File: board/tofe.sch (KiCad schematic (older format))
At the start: 14 parts

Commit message: Moving I2C enable pins to make IO1 a NC.
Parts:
- removed PDG0: DEBUG, CON-SMD-2.54:TE-AMPMODU-MOD-II-4X2, symbol CONN_02X04
- added DDG3: LED, LEDs:LED_0805, symbol LED
- added PDG0: DEBUG, symbol CONN_02X05
- added RDG3: 68R, Resistors_SMD:R_0805_HandSoldering, symbol R
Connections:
- wire segments 136 -> 146
- no-connect marks 4 -> 5

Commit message: Updating PCB.
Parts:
- PDG0: footprint (none) -> Pin_Headers:Pin_Header_Straight_2x05
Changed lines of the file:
@@
 F 0 "PDG0" H 7050 3450 50  0000 C CNN
 F 1 "DEBUG" H 7050 2850 50  0000 C CNN
-F 2 "" H 7050 1950 50  0000 C CNN
+F 2 "Pin_Headers:Pin_Header_Straight_2x05" H 7050 1950 50  0001 C CNN
 F 3 "" H 7050 1950 50  0000 C CNN
 	1    7050 3150

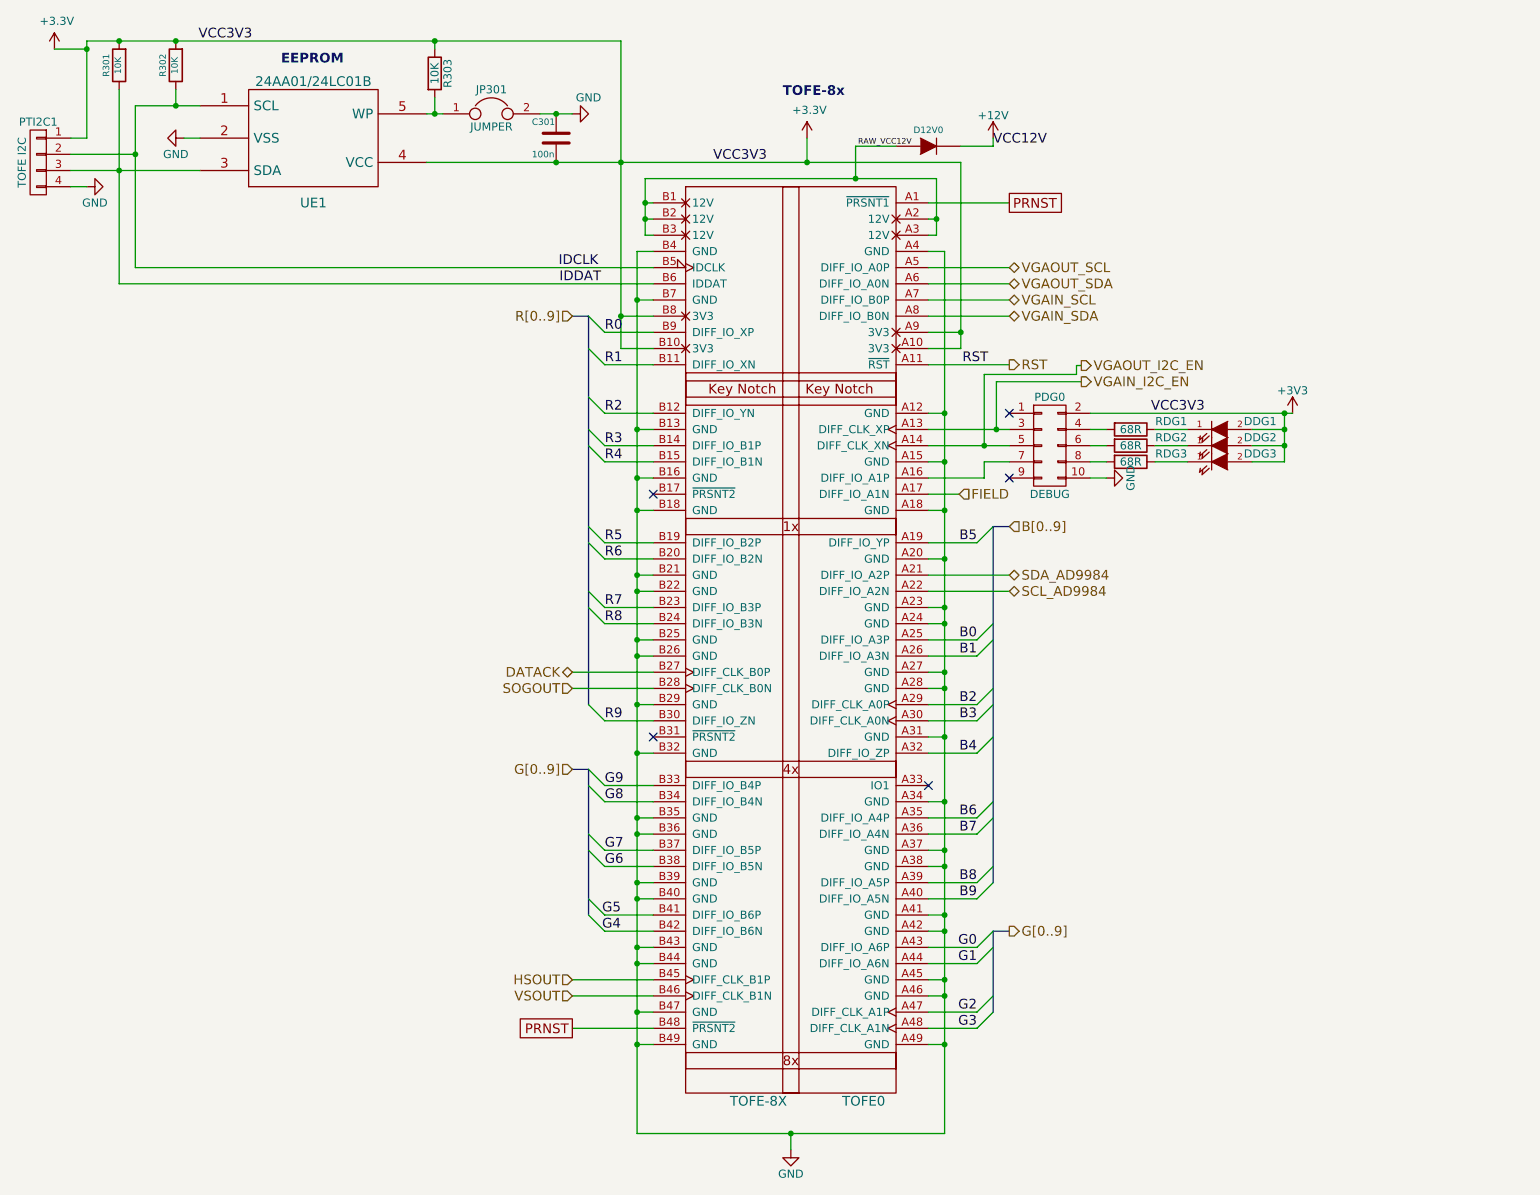
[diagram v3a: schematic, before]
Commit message: Change TOFE connections as per changes requested for PCB design
Note: `DATACK` & `SOGOUT` have been swapped from the original request
      keeping in mind compatibilty for 7-series boards. Please swap them
      back again if absolutely required.
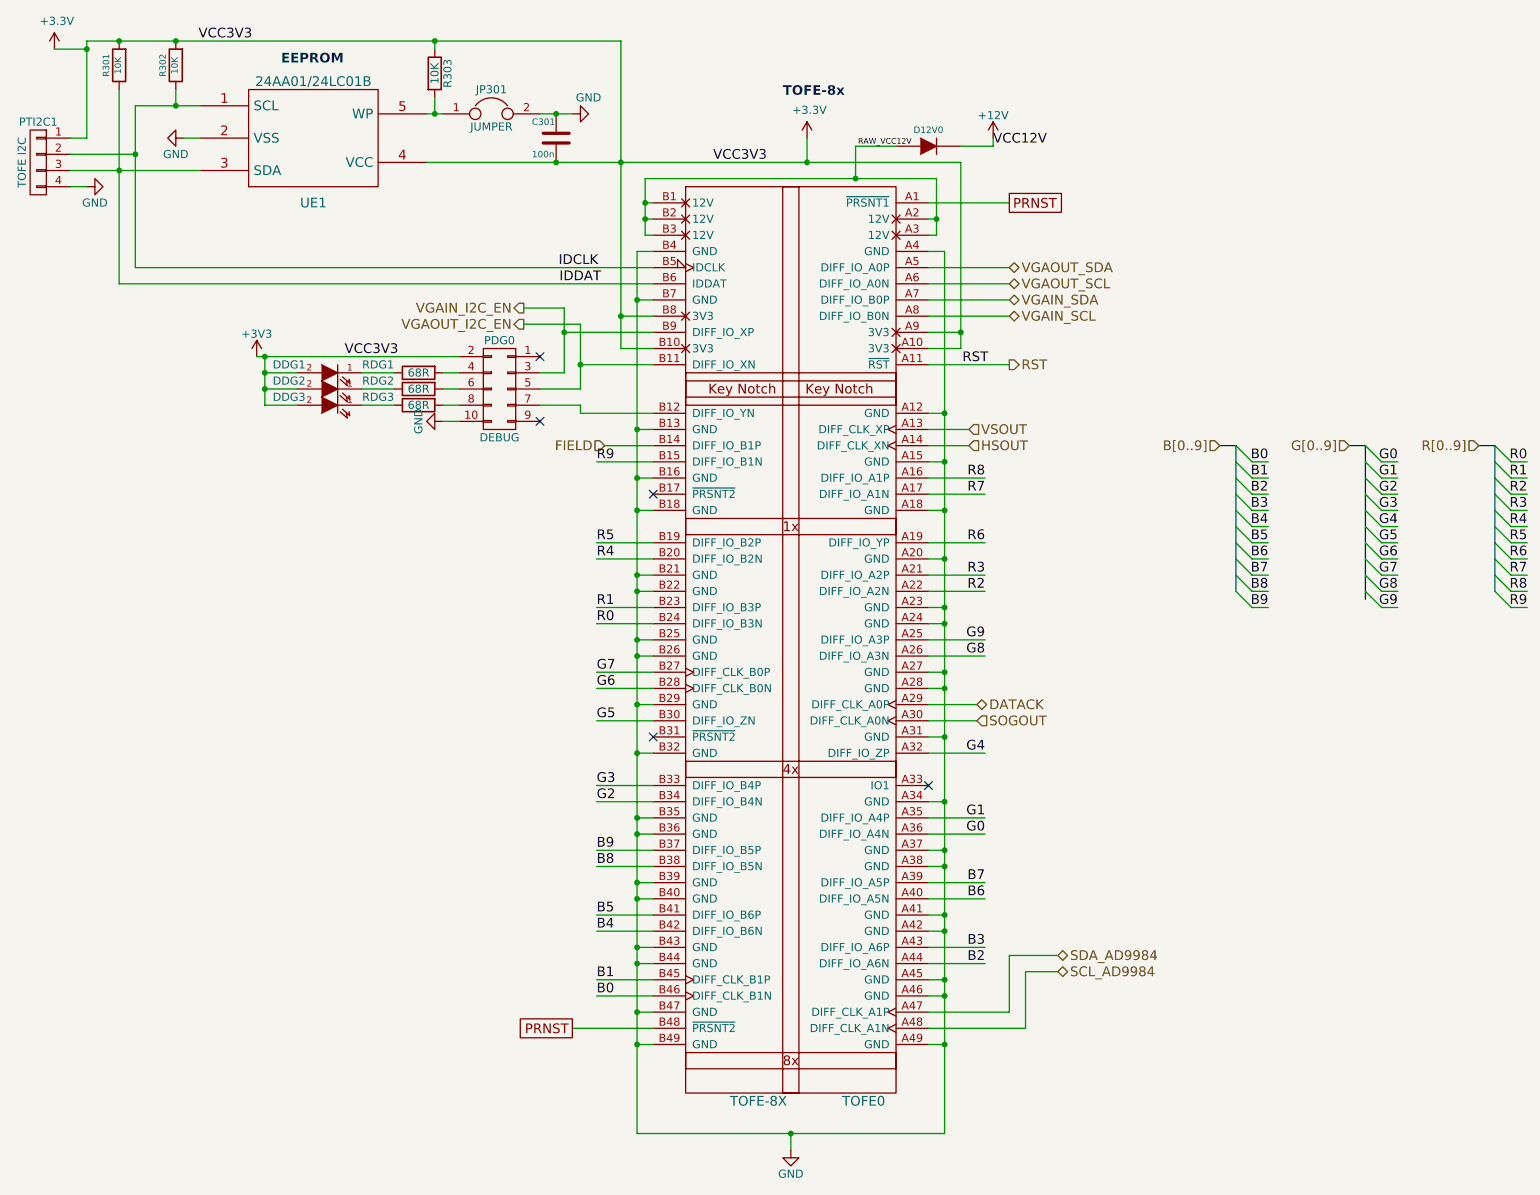
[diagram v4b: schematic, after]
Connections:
- net B0: now also TOFE0.B46 (DIFF_CLK_B1N); no longer TOFE0.A25 (DIFF_IO_A3P)
- net B1: now also TOFE0.B45 (DIFF_CLK_B1P); no longer TOFE0.A26 (DIFF_IO_A3N)
- net B2: now also TOFE0.A44 (DIFF_IO_A6N); no longer TOFE0.A29 (DIFF_CLK_A0P)
- net B3: now also TOFE0.A43 (DIFF_IO_A6P); no longer TOFE0.A30 (DIFF_CLK_A0N)
- net B4: now also TOFE0.B42 (DIFF_IO_B6N); no longer TOFE0.A32 (DIFF_IO_ZP)
- net B5: now also TOFE0.B41 (DIFF_IO_B6P); no longer TOFE0.A19 (DIFF_IO_YP)
- net B6: now also TOFE0.A40 (DIFF_IO_A5N); no longer TOFE0.A35 (DIFF_IO_A4P)
- net B7: now also TOFE0.A39 (DIFF_IO_A5P); no longer TOFE0.A36 (DIFF_IO_A4N)
- net B8: now also TOFE0.B38 (DIFF_IO_B5N); no longer TOFE0.A39 (DIFF_IO_A5P)
- net B9: now also TOFE0.B37 (DIFF_IO_B5P); no longer TOFE0.A40 (DIFF_IO_A5N)
- net DATACK: now also TOFE0.A29 (DIFF_CLK_A0P); no longer TOFE0.B27 (DIFF_CLK_B0P)
- net FIELD: now also TOFE0.B14 (DIFF_IO_B1P); no longer TOFE0.A17 (DIFF_IO_A1N)
- net G0: now also TOFE0.A36 (DIFF_IO_A4N); no longer TOFE0.A43 (DIFF_IO_A6P)
- net G1: now also TOFE0.A35 (DIFF_IO_A4P); no longer TOFE0.A44 (DIFF_IO_A6N)
- net G2: now also TOFE0.B34 (DIFF_IO_B4N); no longer TOFE0.A47 (DIFF_CLK_A1P)
- net G3: now also TOFE0.B33 (DIFF_IO_B4P); no longer TOFE0.A48 (DIFF_CLK_A1N)
- net G4: now also TOFE0.A32 (DIFF_IO_ZP); no longer TOFE0.B42 (DIFF_IO_B6N)
- net G5: now also TOFE0.B30 (DIFF_IO_ZN); no longer TOFE0.B41 (DIFF_IO_B6P)
- net G6: now also TOFE0.B28 (DIFF_CLK_B0N); no longer TOFE0.B38 (DIFF_IO_B5N)
- net G7: now also TOFE0.B27 (DIFF_CLK_B0P); no longer TOFE0.B37 (DIFF_IO_B5P)
- net G8: now also TOFE0.A26 (DIFF_IO_A3N); no longer TOFE0.B34 (DIFF_IO_B4N)
- net G9: now also TOFE0.A25 (DIFF_IO_A3P); no longer TOFE0.B33 (DIFF_IO_B4P)
- net HSOUT: now also TOFE0.A14 (DIFF_CLK_XN); no longer TOFE0.B45 (DIFF_CLK_B1P)
- net R0: now also TOFE0.B24 (DIFF_IO_B3N); no longer TOFE0.B9 (DIFF_IO_XP)
- net R1: now also TOFE0.B23 (DIFF_IO_B3P); no longer TOFE0.B11 (DIFF_IO_XN)
- net R2: now also TOFE0.A22 (DIFF_IO_A2N); no longer TOFE0.B12 (DIFF_IO_YN)
- net R3: now also TOFE0.A21 (DIFF_IO_A2P); no longer TOFE0.B14 (DIFF_IO_B1P)
- net R4: now also TOFE0.B20 (DIFF_IO_B2N); no longer TOFE0.B15 (DIFF_IO_B1N)
- net R6: now also TOFE0.A19 (DIFF_IO_YP); no longer TOFE0.B20 (DIFF_IO_B2N)
- net R7: now also TOFE0.A17 (DIFF_IO_A1N); no longer TOFE0.B23 (DIFF_IO_B3P)
- net R8: now also TOFE0.A16 (DIFF_IO_A1P); no longer TOFE0.B24 (DIFF_IO_B3N)
- net R9: now also TOFE0.B15 (DIFF_IO_B1N); no longer TOFE0.B30 (DIFF_IO_ZN)
- net SCL_AD9984: now also TOFE0.A48 (DIFF_CLK_A1N); no longer TOFE0.A22 (DIFF_IO_A2N)
- net SDA_AD9984: now also TOFE0.A47 (DIFF_CLK_A1P); no longer TOFE0.A21 (DIFF_IO_A2P)
- net SOGOUT: now also TOFE0.A30 (DIFF_CLK_A0N); no longer TOFE0.B28 (DIFF_CLK_B0N)
- net VGAIN_I2C_EN: now also TOFE0.B9 (DIFF_IO_XP); no longer TOFE0.A13 (DIFF_CLK_XP)
- net VGAIN_SCL: now also TOFE0.A8 (DIFF_IO_B0N); no longer TOFE0.A7 (DIFF_IO_B0P)
- net VGAIN_SDA: now also TOFE0.A7 (DIFF_IO_B0P); no longer TOFE0.A8 (DIFF_IO_B0N)
- net VGAOUT_I2C_EN: now also TOFE0.B11 (DIFF_IO_XN); no longer TOFE0.A14 (DIFF_CLK_XN)
- net VGAOUT_SCL: now also TOFE0.A6 (DIFF_IO_A0N); no longer TOFE0.A5 (DIFF_IO_A0P)
- net VGAOUT_SDA: now also TOFE0.A5 (DIFF_IO_A0P); no longer TOFE0.A6 (DIFF_IO_A0N)
- net VSOUT: now also TOFE0.A13 (DIFF_CLK_XP); no longer TOFE0.B46 (DIFF_CLK_B1N)
- net at PDG0.7 (P7): now also TOFE0.B12 (DIFF_IO_YN); no longer TOFE0.A16 (DIFF_IO_A1P)
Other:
- moved on the sheet: DDG1, DDG2, DDG3, PDG0, RDG1, RDG2, RDG3

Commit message: Lots of small fixes to the schematic.
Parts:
- added DDG4: LED, LEDs:LED_0805, symbol LED
- added RDG4: 68R, Resistors_SMD:R_0805_HandSoldering, symbol R
- PDG0: symbol CONN_02X05 -> CONN_02X06
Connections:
- net +3V3: now also PDG0.11 (P11), PDG0.12 (P12), DDG4.2 (A); no longer PDG0.2 (P2)
- net GND: now also PDG0.9 (P9)
- net IDDAT: now also PDG0.1 (P1)
- net at RDG1.2: now also PDG0.2 (P2); no longer PDG0.4 (P4)
- net at RDG2.2: now also PDG0.4 (P4); no longer PDG0.6 (P6)
- net at RDG3.2: now also PDG0.6 (P6); no longer PDG0.8 (P8)
- net VGAIN_I2C_EN: no longer names the net of PDG0.3 (P3), TOFE0.B9 (DIFF_IO_XP)
- net VGAOUT_I2C_EN: no longer names the net of PDG0.5 (P5), TOFE0.B11 (DIFF_IO_XN)
- new net: PDG0.8 (P8), RDG4.2
- new net: DDG4.1 (K), RDG4.1
- no-connect marks 5 -> 3
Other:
- moved on the sheet: DDG1, DDG2, DDG3, RDG1, RDG2, RDG3

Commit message: Lots of small fixes.
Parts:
- PDG0: footprint Pin_Headers:Pin_Header_Straight_2x05 -> Pin_Headers:Pin_Header_Straight_2x06
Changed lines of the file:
@@
 F 0 "PDG0" H 3650 3225 50  0000 C CNN
 F 1 "DEBUG" H 3650 2500 50  0000 C CNN
-F 2 "Pin_Headers:Pin_Header_Straight_2x05" H 3650 1650 50  0001 C CNN
+F 2 "Pin_Headers:Pin_Header_Straight_2x06" H 3650 1650 50  0001 C CNN
 F 3 "" H 3650 1650 50  0000 C CNN
 	1    3650 2850
@@
 	4600 1950 4500 1950
 Wire Wire Line
-	4500 1950 4500 2250
-Wire Wire Line
-	4500 2250 4500 3050
-Wire Wire Line
-	4500 3050 4500 3350
-Wire Wire Line
-	4500 3350 4500 3550
-Wire Wire Line
-	4500 3550 4500 3950
-Wire Wire Line
-	4500 3950 4500 4050
-Wire Wire Line
-	4500 4050 4500 4350
-Wire Wire Line
-	4500 4350 4500 4450
-Wire Wire Line
-	4500 4450 4500 4750
-Wire Wire Line
-	4500 4750 4500 5050
-Wire Wire Line
-	4500 5050 4500 5450
-Wire Wire Line
-	4500 5450 4500 5550
-Wire Wire Line
-	4500 5550 4500 5850
-Wire Wire Line
-	4500 5850 4500 5950
-Wire Wire Line
-	4500 5950 4500 6250
-Wire Wire Line
-	4500 6250 4500 6350
-Wire Wire Line
-	4500 6350 4500 6650
-Wire Wire Line
-	4500 6650 4500 6850
-Wire Wire Line
-	4500 6850 4500 7400
+	4500 1950 4500 7400
 Wire Wire Line
 	4500 2250 4600 2250
@@
 Connection ~ 6400 6550
 Wire Wire Line
-	4500 7400 5450 7400
-Wire Wire Line
-	5450 7400 6400 7400
+	4500 7400 6400 7400
 Connection ~ 4500 6850
 Connection ~ 6400 6850
@@
 	4400 2550 4600 2550
 Wire Wire Line
-	4400 650  4400 1400
-Wire Wire Line
-	4400 1400 4400 2350
-Wire Wire Line
-	4400 2350 4400 2550
+	4400 650  4400 2550
 Wire Wire Line
 	4400 2350 4600 2350
@@
 	6300 2450 6500 2450
 Wire Wire Line
-	6500 1400 6500 2450
-Wire Wire Line
-	6500 2450 6500 2550
+	6500 1400 6500 2550
 Wire Wire Line
 	6500 2550 6300 2550
 Wire Wire Line
-	3200 1400 4000 1400
-Wire Wire Line
-	4000 1400 4400 1400
-Wire Wire Line
-	4400 1400 5550 1400
-Wire Wire Line
-	5550 1400 6500 1400
+	3200 1400 6500 1400
 Connection ~ 6500 2450
 Connection ~ 4400 2350
@@
 	4550 1850 4600 1850
 Wire Wire Line
-	4550 1500 4550 1650
-Wire Wire Line
-	4550 1650 4550 1750
-Wire Wire Line
-	4550 1750 4550 1850
+	4550 1500 4550 1850
 Wire Wire Line
 	4550 1750 4600 1750
@@
 	6350 1850 6300 1850
 Wire Wire Line
-	6350 1500 6350 1750
-Wire Wire Line
-	6350 1750 6350 1850
+	6350 1500 6350 1850
 Wire Wire Line
 	6350 1750 6300 1750
 Wire Wire Line
-	4550 1500 5850 1500
-Wire Wire Line
-	5850 1500 6350 1500
+	4550 1500 6350 1500
 Connection ~ 6350 1750
 Connection ~ 4550 1650
@@
 Connection ~ 4000 1400
 Wire Wire Line
-	6400 7400 6400 6850
-Wire Wire Line
-	6400 6850 6400 6550
-Wire Wire Line
-	6400 6550 6400 6450
-Wire Wire Line
-	6400 6450 6400 6150
-Wire Wire Line
-	6400 6150 6400 6050
-Wire Wire Line
-	6400 6050 6400 5750
-Wire Wire Line
-	6400 5750 6400 5650
-Wire Wire Line
-	6400 5650 6400 5350
-Wire Wire Line
-	6400 5350 6400 4950
-Wire Wire Line
-	6400 4950 6400 4650
-Wire Wire Line
-	6400 4650 6400 4550
-Wire Wire Line
-	6400 4550 6400 4250
-Wire Wire Line
-	6400 4250 6400 4150
-Wire Wire Line
-	6400 4150 6400 3850
-Wire Wire Line
-	6400 3850 6400 3550
-Wire Wire Line
-	6400 3550 6400 3250
-Wire Wire Line
-	6400 3250 6400 2950
-Wire Wire Line
-	6400 2950 6400 1950
+	6400 7400 6400 1950
 Wire Wire Line
 	1400 2050 4600 2050
 Wire Wire Line
-	1300 2150 3975 2150
-Wire Wire Line
-	3975 2150 4600 2150
-Wire Wire Line
-	3900 1100 4000 1100
-Wire Wire Line
-	4000 1100 4100 1100
+	1300 2150 4600 2150
+Wire Wire Line
+	3900 1100 4100 1100
 Wire Wire Line
 	1700 1250 1800 1250
@@
 	1650 950  1650 1050
 Wire Wire Line
-	1400 1050 1650 1050
-Wire Wire Line
-	1650 1050 1800 1050
-Wire Wire Line
-	1000 1450 1300 1450
-Wire Wire Line
-	1300 1450 1800 1450
+	1400 1050 1800 1050
+Wire Wire Line
+	1000 1450 1800 1450
 Connection ~ 4000 1100
 Wire Wire Line
-	1400 1050 1400 1350
-Wire Wire Line
-	1400 1350 1400 2050
+	1400 1050 1400 2050
 Connection ~ 1650 1050
 Wire Wire Line
-	1100 650  1300 650
-Wire Wire Line
-	1300 650  1650 650
-Wire Wire Line
-	1650 650  3250 650
-Wire Wire Line
-	3250 650  4400 650
+	1100 650  4400 650
 Connection ~ 4400 1400
 Connection ~ 1650 650
@@
 	9700 3150 9800 3150
 Wire Bus Line
-	9800 3150 9800 3250
-Wire Bus Line
-	9800 3250 9800 3350
-Wire Bus Line
-	9800 3350 9800 3450
-Wire Bus Line
-	9800 3450 9800 3550
-Wire Bus Line
-	9800 3550 9800 3650
-Wire Bus Line
-	9800 3650 9800 3750
-Wire Bus Line
-	9800 3750 9800 3850
-Wire Bus Line
-	9800 3850 9800 3950
-Wire Bus Line
-	9800 3950 9800 4050
+	9800 3150 9800 4050
 Wire Bus Line
 	8900 3150 9000 3150
 Wire Bus Line
-	9000 3150 9000 3250
-Wire Bus Line
-	9000 3250 9000 3350
-Wire Bus Line
-	9000 3350 9000 3450
-Wire Bus Line
-	9000 3450 9000 3550
-Wire Bus Line
-	9000 3550 9000 3650
-Wire Bus Line
-	9000 3650 9000 3750
-Wire Bus Line
-	9000 3750 9000 3850
-Wire Bus Line
-	9000 3850 9000 3950
-Wire Bus Line
-	9000 3950 9000 4050
-Wire Bus Line
-	9000 4050 9000 4100
+	9000 3150 9000 4100
 Wire Wire Line
 	6300 5950 6650 5950
@@
 	9200 3550 9100 3550
 Wire Bus Line
-	8200 3150 8200 3250
-Wire Bus Line
-	8200 3250 8200 3350
-Wire Bus Line
-	8200 3350 8200 3450
-Wire Bus Line
-	8200 3450 8200 3550
-Wire Bus Line
-	8200 3550 8200 3650
-Wire Bus Line
-	8200 3650 8200 3750
-Wire Bus Line
-	8200 3750 8200 3850
-Wire Bus Line
-	8200 3850 8200 3950
-Wire Bus Line
-	8200 3950 8200 4050
+	8200 3150 8200 4050
 Wire Wire Line
 	6300 3950 6650 3950
@@
 	6300 4050 6650 4050
 Wire Wire Line
-	3200 1100 3250 1100
-Wire Wire Line
-	3250 1100 3300 1100
-Wire Wire Line
-	1300 950  1300 1450
-Wire Wire Line
-	1300 1450 1300 2150
+	3200 1100 3300 1100
+Wire Wire Line
+	1300 950  1300 2150
 Connection ~ 1300 1450
 Wire Wire Line
@@
 Connection ~ 2200 2600
 Wire Wire Line
-	1100 650  1100 700
-Wire Wire Line
-	1100 700  1100 1250
+	1100 650  1100 1250
 Wire Wire Line
 	1100 1250 1000 1250
@@
 	2200 2800 2400 2800
 Wire Wire Line
-	2200 2550 2200 2600
-Wire Wire Line
-	2200 2600 2200 2700
-Wire Wire Line
-	2200 2700 2200 2800
-Wire Wire Line
-	2200 2800 2200 2900
-Wire Wire Line
-	2200 2900 2200 3100
-Wire Wire Line
-	3075 3000 3275 3000
-Wire Wire Line
-	3275 3000 3400 3000
+	2200 2550 2200 3100
+Wire Wire Line
+	3075 3000 3400 3000
 Wire Wire Line
 	4150 2650 4600 2650
@@
 	4150 2650 4150 2800
 Wire Wire Line
-	2200 3100 3350 3100
-Wire Wire Line
-	3350 3100 3400 3100
+	2200 3100 3400 3100
 Connection ~ 2200 2800
 Wire Wire Line

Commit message: Fixing the footprint for lots of things.
 * Capacitors 0805 or can.
 * Resistors 0603.
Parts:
- C301: footprint Resistors_SMD:R_0805_HandSoldering -> Capacitors_SMD:C_0805_HandSoldering
- R301, R302, R303, RDG1, RDG2, RDG3, RDG4: footprint Resistors_SMD:R_0805_HandSoldering -> Resistors_SMD:R_0603_HandSoldering
- TOFE0: footprint TOFE_8X_HalfHeight:TOFE_8X_HalfHeight -> TOFE_8X_FullHeight:TOFE_8X_FullHeight
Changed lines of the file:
@@
 F 0 "TOFE0" H 5900 1500 60  0000 C CNN
 F 1 "TOFE-8X" H 5250 1500 60  0000 C CNN
-F 2 "TOFE_8X_HalfHeight:TOFE_8X_HalfHeight" H 4600 4050 60  0001 C CNN
+F 2 "TOFE_8X_FullHeight:TOFE_8X_FullHeight" H 4600 4050 60  0001 C CNN
 F 3 "~" H 4600 4050 60  0000 C CNN
 	1    5900 4350
@@
 F 0 "R302" V 1730 800 40  0000 C CNN
 F 1 "10K" V 1657 801 40  0000 C CNN
-F 2 "Resistors_SMD:R_0805_HandSoldering" V 1580 800 30  0001 C CNN
+F 2 "Resistors_SMD:R_0603_HandSoldering" V 1580 800 30  0001 C CNN
 F 3 "~" H 1650 800 30  0000 C CNN
 	1    1650 800
@@
 F 0 "R301" V 1380 800 40  0000 C CNN
 F 1 "10K" V 1307 801 40  0000 C CNN
-F 2 "Resistors_SMD:R_0805_HandSoldering" V 1230 800 30  0001 C CNN
+F 2 "Resistors_SMD:R_0603_HandSoldering" V 1230 800 30  0001 C CNN
 F 3 "~" H 1300 800 30  0000 C CNN
 	1    1300 800
@@
 F 0 "C301" H 3850 1350 40  0000 L CNN
 F 1 "100n" H 3850 1150 40  0000 L CNN
-F 2 "Resistors_SMD:R_0805_HandSoldering" H 4038 1100 30  0001 C CNN
+F 2 "Capacitors_SMD:C_0805_HandSoldering" H 4038 1100 30  0001 C CNN
 F 3 "~" H 4000 1250 60  0000 C CNN
 	1    4000 1250
@@
 F 0 "RDG1" V 3100 2850 50  0000 C CNN
 F 1 "68R" V 3150 2600 50  0000 C CNN
-F 2 "Resistors_SMD:R_0805_HandSoldering" V 3080 2600 50  0001 C CNN
+F 2 "Resistors_SMD:R_0603_HandSoldering" V 3080 2600 50  0001 C CNN
 F 3 "" H 3150 2600 50  0000 C CNN
 	1    3150 2600
@@
 F 0 "RDG2" V 3100 2950 50  0000 C CNN
 F 1 "68R" V 3150 2700 50  0000 C CNN
-F 2 "Resistors_SMD:R_0805_HandSoldering" V 3080 2700 50  0001 C CNN
+F 2 "Resistors_SMD:R_0603_HandSoldering" V 3080 2700 50  0001 C CNN
 F 3 "" H 3150 2700 50  0000 C CNN
 	1    3150 2700
@@
 F 0 "R303" V 3330 850 50  0000 C CNN
 F 1 "10K" V 3250 850 50  0000 C CNN
-F 2 "Resistors_SMD:R_0805_HandSoldering" V 3180 850 50  0001 C CNN
+F 2 "Resistors_SMD:R_0603_HandSoldering" V 3180 850 50  0001 C CNN
 F 3 "" H 3250 850 50  0000 C CNN
 	1    3250 850
@@
 F 0 "RDG3" V 3100 3050 50  0000 C CNN
 F 1 "68R" V 3150 2800 50  0000 C CNN
-F 2 "Resistors_SMD:R_0805_HandSoldering" V 3080 2800 50  0001 C CNN
+F 2 "Resistors_SMD:R_0603_HandSoldering" V 3080 2800 50  0001 C CNN
 F 3 "" H 3150 2800 50  0000 C CNN
 	1    3150 2800
@@
 F 0 "RDG4" V 3100 3150 50  0000 C CNN
 F 1 "68R" V 3150 2900 50  0000 C CNN
-F 2 "Resistors_SMD:R_0805_HandSoldering" V 3080 2900 50  0001 C CNN
+F 2 "Resistors_SMD:R_0603_HandSoldering" V 3080 2900 50  0001 C CNN
 F 3 "" H 3150 2900 50  0000 C CNN
 	1    3150 2900

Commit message: Import and update netlist.
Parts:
- TOFE0: footprint TOFE_8X_FullHeight:TOFE_8X_FullHeight -> TOFE_8X_HalfHeight:TOFE_8X_HalfHeight
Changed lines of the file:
@@
 F 0 "TOFE0" H 5900 1500 60  0000 C CNN
 F 1 "TOFE-8X" H 5250 1500 60  0000 C CNN
-F 2 "TOFE_8X_FullHeight:TOFE_8X_FullHeight" H 4600 4050 60  0001 C CNN
+F 2 "TOFE_8X_HalfHeight:TOFE_8X_HalfHeight" H 4600 4050 60  0001 C CNN
 F 3 "~" H 4600 4050 60  0000 C CNN
 	1    5900 4350
